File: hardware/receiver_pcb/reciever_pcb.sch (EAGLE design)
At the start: 17 parts

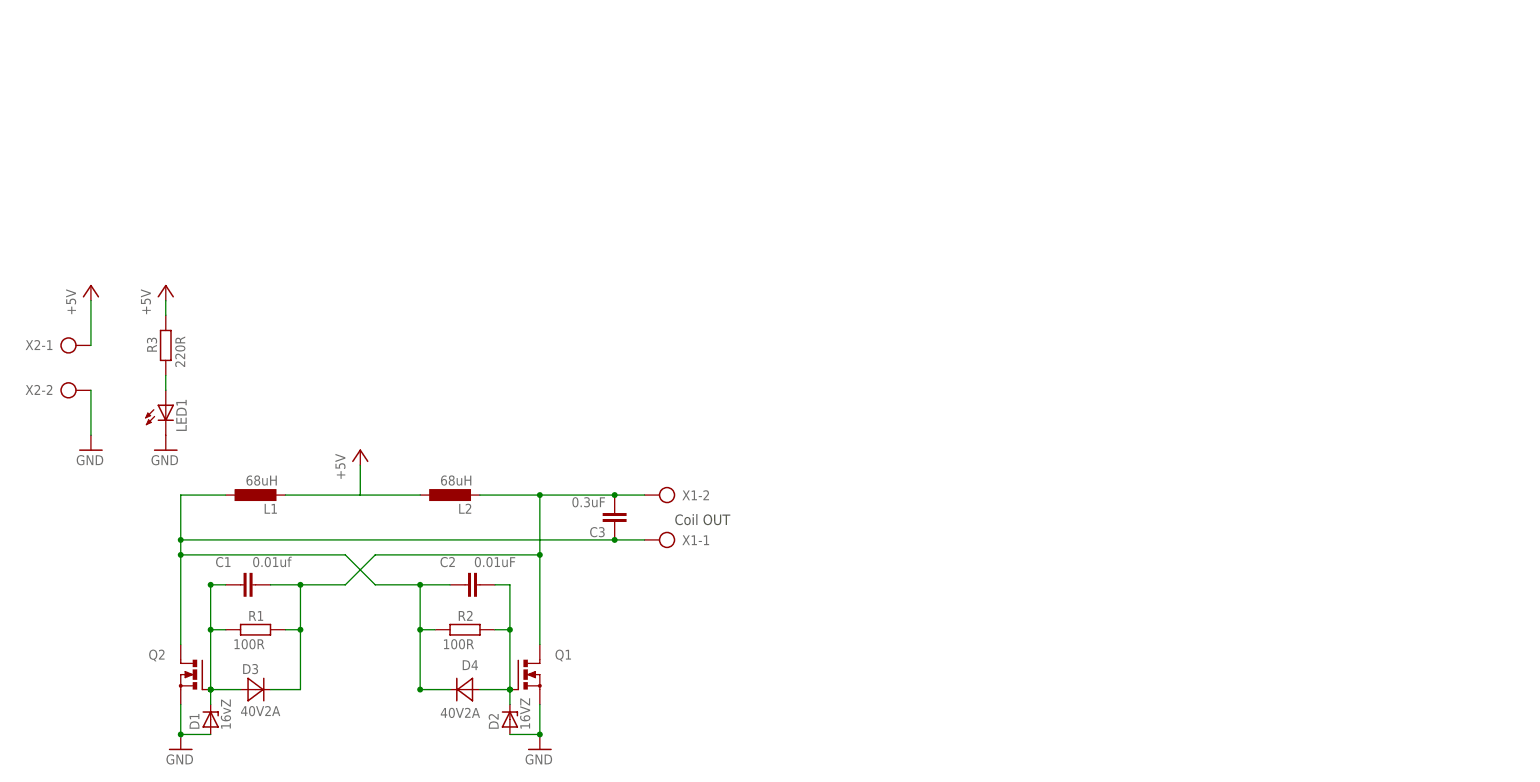
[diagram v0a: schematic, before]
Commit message: better dir struct, and some tweaks to pcbs
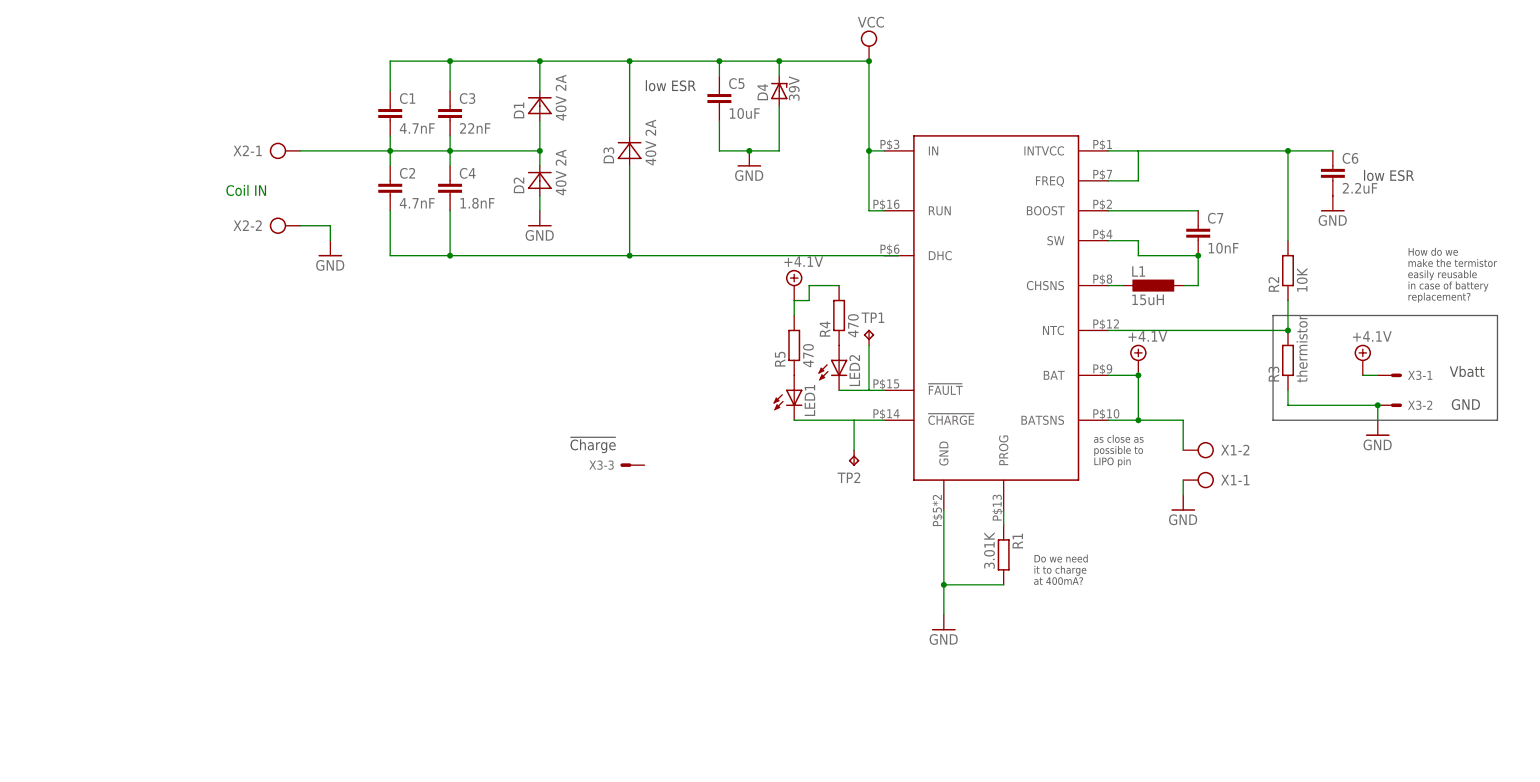
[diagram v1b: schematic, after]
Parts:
- removed L2: 68uH, rcl:L-EUL5650M
- removed Q1, Q2: (no value), transistor-power:N-MOSFET-SO8S
- added C4: 1.8nF, rcl:C-EUC0805
- added C5: 10uF, rcl:C-EUC0805
- added C6: 2.2uF, rcl:C-EUC0805
- added C7: 10nF, rcl:C-EUC0805
- added LED2: (no value), led:LEDCHIP-LED0805
- added R4, R5: 470, rcl:R-EU_R0805
- added TP1, TP2: TPTP19R, testpad:TPTP19R
- added U$1: LT4120, custom parts:LT4120
- added X3: (no value), con-molex:KK-156-3
- C1: value 0.01uf -> 4.7nF
- C2: value 0.01uF -> 4.7nF
- C3: value 0.3uF -> 22nF
- D1: value 16vZ -> 40V 2A; device diode:ZENER-DIODESOD80C -> diode:MBRA340T3
- D2: value 16VZ -> 40V 2A; device diode:ZENER-DIODESOD80C -> diode:MBRA340T3
- D3: value 40V2A -> 40V 2A
- D4: value 40V2A -> 39V; device diode:MBRA340T3 -> diode:ZENER-DIODESMB
- L1: value 68uH -> 15uH; device rcl:L-EUL5650M -> rcl:L-EUL1812
- R1: value 100R -> 3.01K
- R2: value 100R -> 10K
- R3: value 220R -> thermistor; device rcl:R-EU_R0805 -> rcl:R-EU_0207/2V
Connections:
- removed net +5V: L1.2, L2.1, R3.2, X2-1.KL
- new net +4.1V: R4.2, R5.2, U$1.BAT, U$1.BATSNS, X1-2.KL, X3-1.S
- new net N$10: LED2.A, R4.1
- new net N$11: LED1.A, R5.1
- new net N$13: LED2.C, TP1.TP, U$1.!FAULT
- new net N$6: L1.2, U$1.CHSNS
- new net N$7: R1.1, U$1.PROG
- new net N$8: R2.1, R3.2, U$1.NTC
- new net N$9: LED1.C, TP2.TP, U$1.!CHARGE
- new net VCC: C1.1, C3.1, C5.1, D1.C, D3.C, D4.C, U$1.IN, U$1.RUN
- net GND: now also C5.2, C6.2, D4.A, R1.2, R3.1, U$1.GND, X1-1.KL, X3-2.S; no longer D1.A, LED1.C, Q1.S, Q2.S
- net N$1: now also C1.2, C2.1, C3.2, C4.1, D1.A, D2.C, X2-1.KL; no longer C1.1, D1.C, D3.A, Q2.G, R1.1
- net N$2: now also C2.2, C4.2, D3.A; no longer C1.2, C3.2, D3.C, L2.2, Q1.D, R1.2, X1-2.KL
- net N$3: now also C6.1, U$1.FREQ, U$1.INTVCC; no longer C2.2, D2.C, D4.A, Q1.G
- net N$4: now also C7.1, U$1.BOOST; no longer C2.1, C3.1, D4.C, L1.1, Q2.D, R2.1, X1-1.KL
- net N$5: now also C7.2, L1.1, U$1.SW; no longer LED1.A, R3.1
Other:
- note added: "!Charge"
- note added: "Coil IN"
- note added: "Do we need it to charge at 400mA?"
- note added: "GND"
- note added: "How do we make the termistor easily reusable in case of battery replacement?"
- note added: "Vbatt"
- note added: "as close as possible to LIPO pin"
- note added: "low ESR"
- note removed: "Coil OUT"
- moved on the sheet: C1, C2, C3, D3, L1, LED1, R1, R2, R3, X1-1, X1-2, X2-1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

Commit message: checkpoints revised with Matt, new footprints
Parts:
- added X5: (no value), con-molex:KK-156-2
- D1, D2, D3: value 40V 2A -> DFLS240L; device diode:MBRA340T3 -> custom parts:DFLS240L
- D4: value 39V -> 39VZ; device diode:ZENER-DIODESMB -> custom parts:DFLS240L
- L1: device rcl:L-EUL1812 -> custom parts:D62LCB
- R3: value thermistor -> 22K; device rcl:R-EU_0207/2V -> pot:TRIM_EU-S63S
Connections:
- new net N$12: R1.2, R3.A
- net GND: now also R3.E, R3.S, X5-1.S; no longer R1.2, R3.1
- net N$1: now also D2.K; no longer D2.C
- net N$2: now also U$1.DHC
- net N$5: now also L1.P$2; no longer L1.1
- net N$6: now also L1.P$1; no longer L1.2
- net N$8: now also X5-2.S; no longer R3.2
- net N$9: now also X3-3.S
- net VCC: now also D1.K, D3.K, D4.K; no longer D1.C, D3.C, D4.C
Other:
- note added: "Thermistor"
- note removed: "Do we need it to charge at 400mA?"
